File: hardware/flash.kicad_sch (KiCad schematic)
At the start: 2 parts, among them U1 ECP5U_12_CABGA256, U11 W25Q128JVS

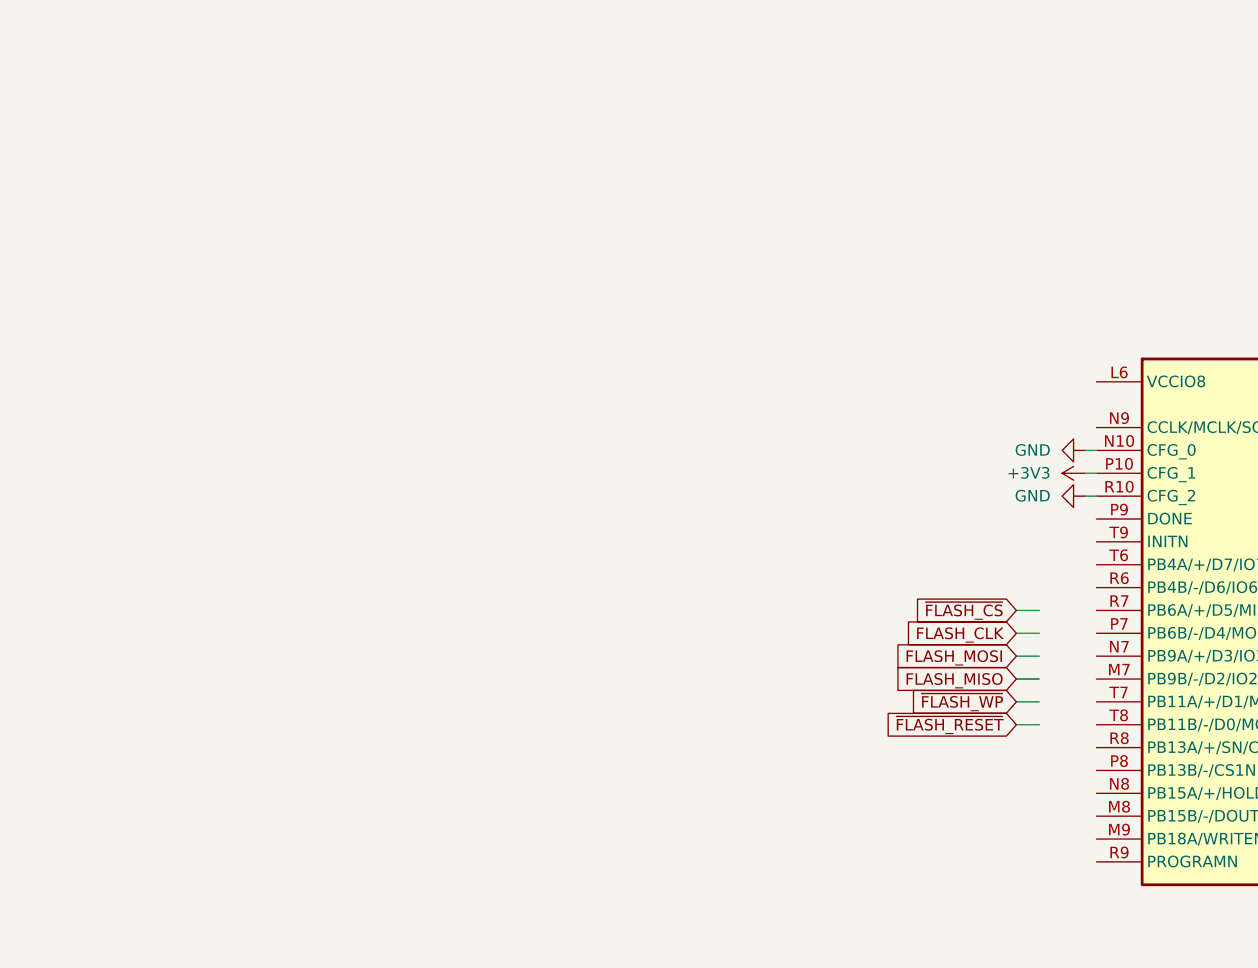
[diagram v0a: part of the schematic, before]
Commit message: Routed most of sdram
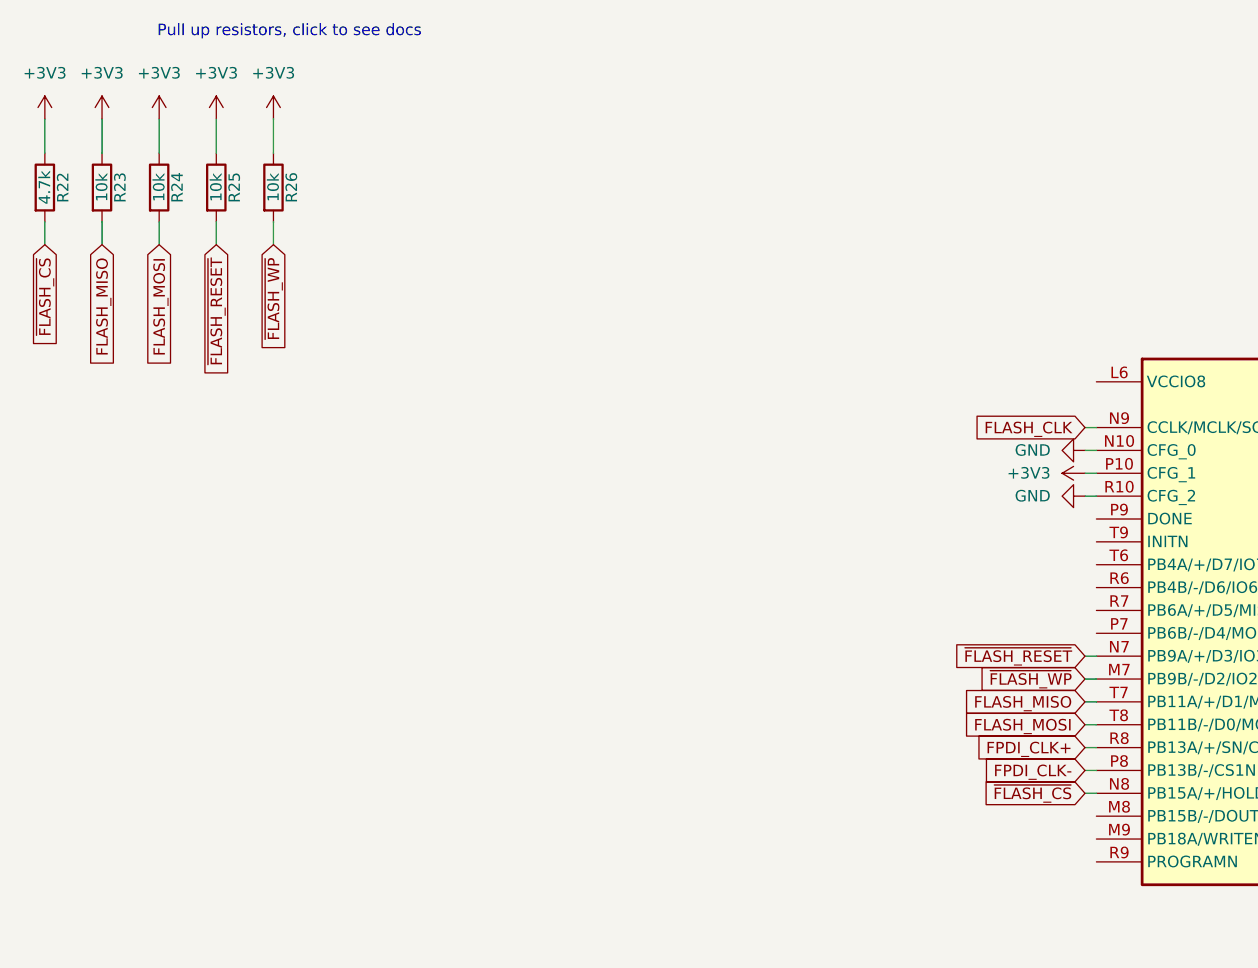
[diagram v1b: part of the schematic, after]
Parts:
- added R22: 4.7k, Resistor_SMD:R_0402_1005Metric, symbol Device:R
- added R23, R24, R25, R26: 10k, Resistor_SMD:R_0402_1005Metric, symbol Device:R
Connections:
- net +3V3: now also R22.1, R23.1, R24.1, R25.1, R26.1
- net FLASH_CLK: now also U1.N9 (CCLK/MCLK/SCK)
- net FLASH_MISO: now also U1.T7 (PB11A/+/D1/MISO/IO1), R23.2
- net FLASH_MOSI: now also U1.T8 (PB11B/-/D0/MOSI/IO0), R24.2
- net ~{FLASH_CS}: now also U1.N8 (PB15A/+/HOLDN/DI/BUSY/CSSPIN/CEN), R22.2
- net ~{FLASH_RESET}: now also U1.N7 (PB9A/+/D3/IO3), R25.2
- net ~{FLASH_WP}: now also U1.M7 (PB9B/-/D2/IO2), R26.2
- net FPDI_CLK-: now reaches U1.P8 (PB13B/-/CS1N)
- net FPDI_CLK+: now reaches U1.R8 (PB13A/+/SN/CSN)
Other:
- note added: "Pull up resistors, click to see docs"

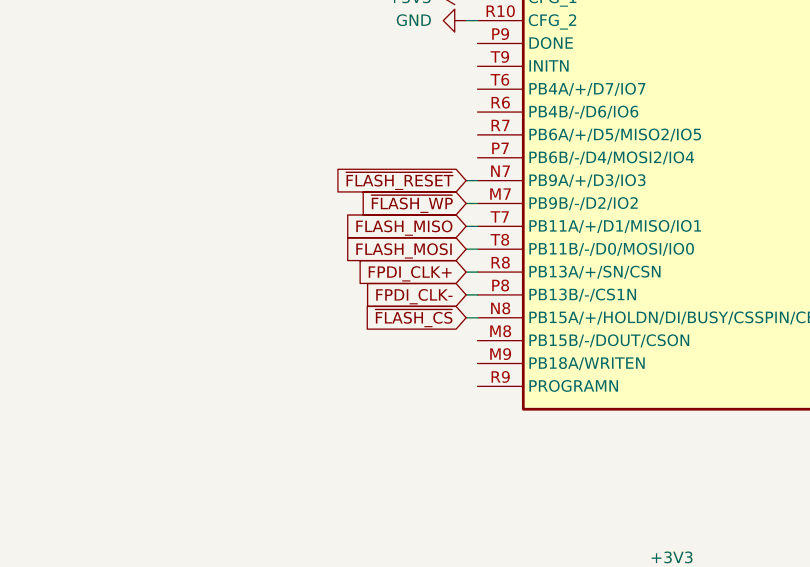
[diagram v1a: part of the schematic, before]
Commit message: Routed power
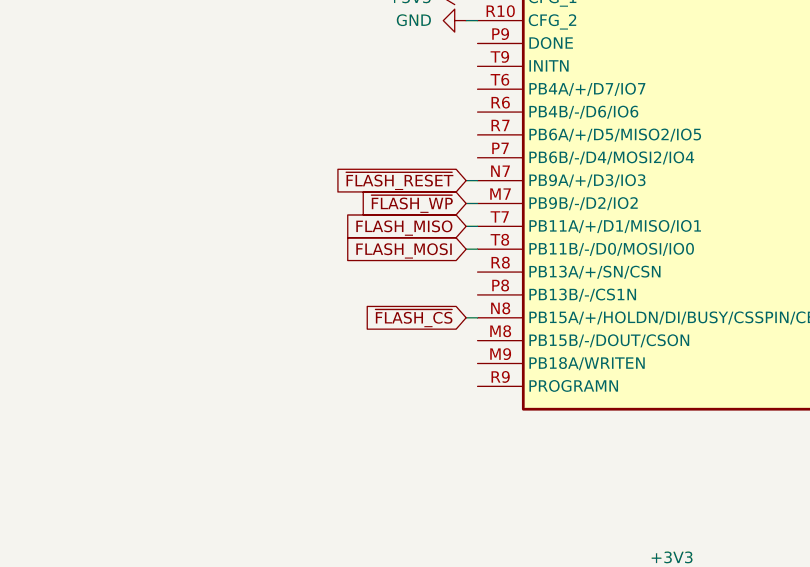
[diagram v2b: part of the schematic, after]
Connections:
- net FPDI_CLK+: no longer names the net of U1.R8 (PB13A/+/SN/CSN)
- net FPDI_CLK-: no longer names the net of U1.P8 (PB13B/-/CS1N)
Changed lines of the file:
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@@
 	(wire
 		(pts
-			(xy 140.97 99.06) (xy 142.24 99.06)
+			(xy 140.97 66.04) (xy 142.24 66.04)
 		)
 		(stroke
@@
 	(wire
 		(pts
-			(xy 140.97 96.52) (xy 142.24 96.52)
+			(xy 151.13 139.7) (xy 153.67 139.7)
 		)
 		(stroke
@@
 	(wire
 		(pts
-			(xy 140.97 66.04) (xy 142.24 66.04)
+			(xy 140.97 63.5) (xy 142.24 63.5)
 		)
 		(stroke
@@
 		)
 	)
-	(wire
-		(pts
-			(xy 151.13 139.7) (xy 153.67 139.7)
-		)
-		(stroke
-			(width 0)
-			(type default)
-		)
-	)
-	(wire
-		(pts
-			(xy 140.97 63.5) (xy 142.24 63.5)
-		)
-		(stroke
-			(width 0)
-			(type default)
-		)
-	)
-	(global_label "FPDI_CLK-"
-		(shape input)
-		(at 140.97 99.06 180)
-		(fields_autoplaced yes)
-		(effects
-			(font
-				(size 1.27 1.27)
-			)
-			(justify right)
-		)
-		(property "Intersheetrefs" "${INTERSHEET_REFS}"
-			(at 127.6433 99.06 0)
-			(effects
-				(font
-					(size 1.27 1.27)
-				)
-				(justify right)
-				(hide yes)
-			)
-		)
-	)
 	(global_label "FLASH_CLK"
 		(shape input)
@@
 			(effects
 				(font
-					(size 1.27 1.27)
-				)
-				(justify right)
-				(hide yes)
-			)
-		)
-	)
-	(global_label "FPDI_CLK+"
-		(shape input)
-		(at 140.97 96.52 180)
-		(fields_autoplaced yes)
-		(effects
-			(font
-				(size 1.27 1.27)
-			)
-			(justify right)
-		)
-		(property "Intersheetrefs" "${INTERSHEET_REFS}"
-			(at 127.6433 96.52 0)
-			(effects
-				(font

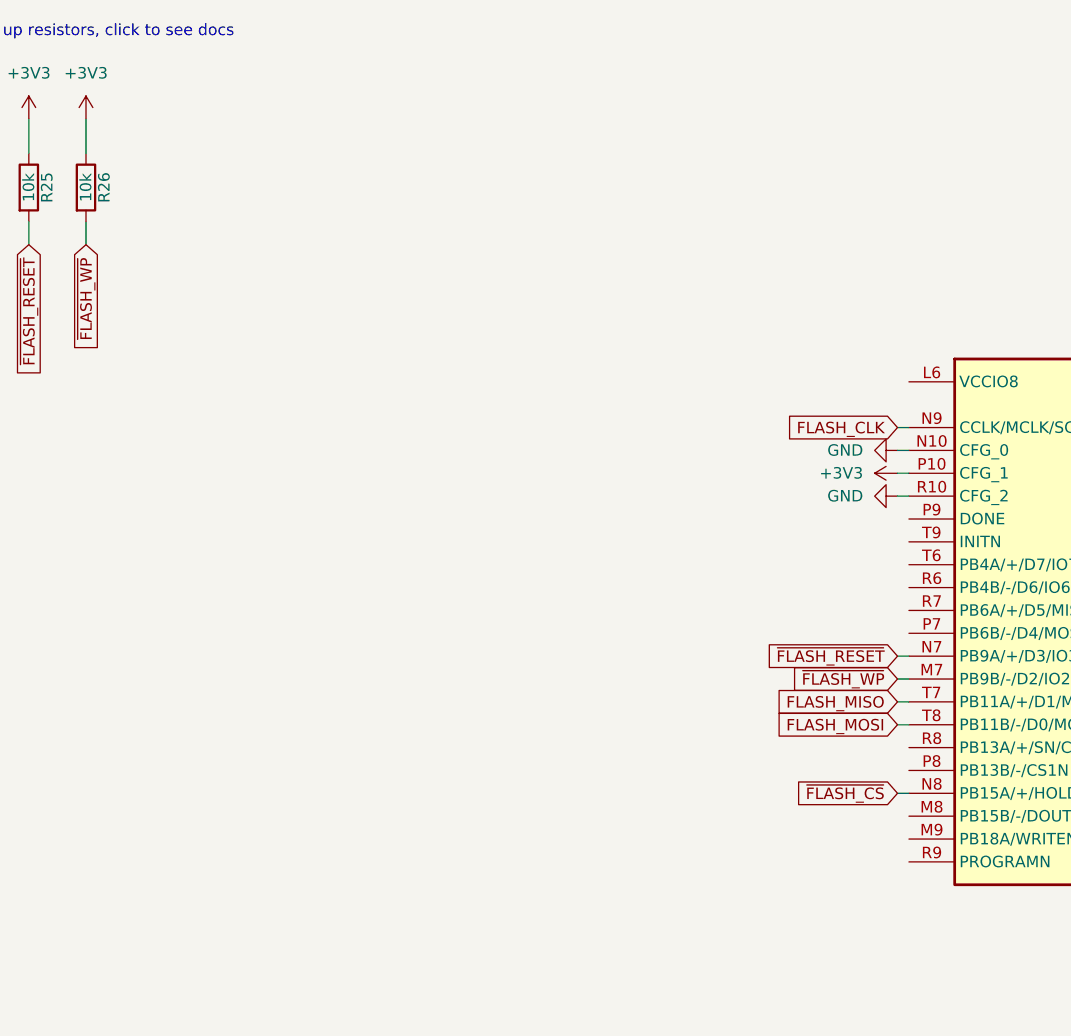
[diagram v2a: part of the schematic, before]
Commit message: Added the decoupling capacitors
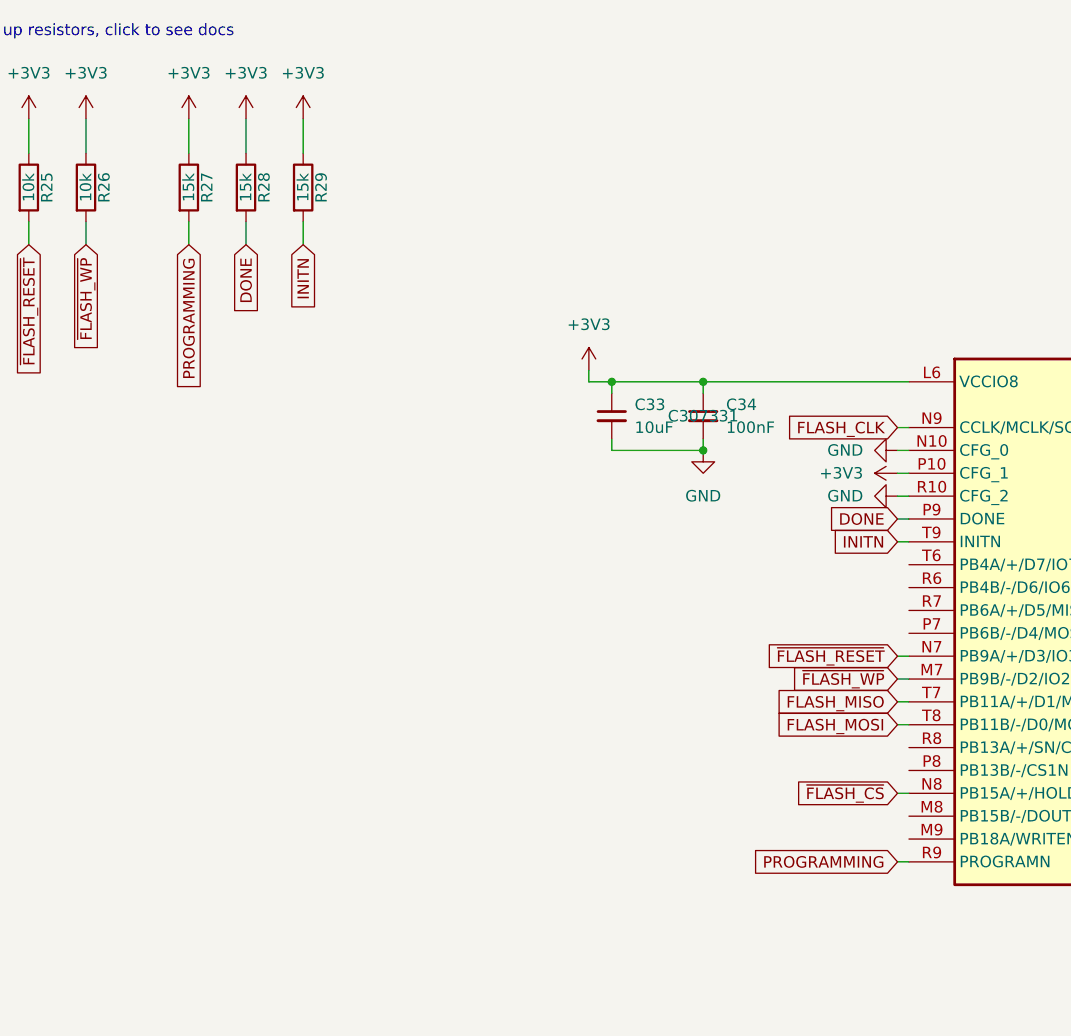
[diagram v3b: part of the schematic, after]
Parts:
- added C33: 10uF, Capacitor_SMD:C_0603_1608Metric, symbol Device:C_Small
- added C34: 100nF, Capacitor_SMD:C_0402_1005Metric, symbol Device:C_Small
- added R27, R28, R29: 15k, Resistor_SMD:R_0402_1005Metric, symbol Device:R
- R22: JLCPCB Part # (none) -> C25900
- R23, R24, R25, R26: JLCPCB Part # (none) -> C25744
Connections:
- net +3V3: now also U1.L6 (VCCIO8), C33.1, C34.1, R27.1, R28.1, R29.1
- net GND: now also C33.2, C34.2
- net DONE: now reaches U1.P9 (DONE)
- net DONE: now also R28.2
- net PROGRAMMING: now reaches U1.R9 (PROGRAMN)
- net PROGRAMMING: now also R27.2
- net INITN: now reaches U1.T9 (INITN)
- net INITN: now also R29.2

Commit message: V1.0 Final Revision and Readme documentation
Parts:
- added C38: 10uF, Capacitor_SMD:C_0603_1608Metric, symbol Device:C_Small
- added J6: Micro_SD_Card_Det2, icepi-lib:microSD_HC_SOFNG_TF-008, symbol Connector:Micro_SD_Card_Det2
- renumbered C33 to C36, C34 to C37, R22 to R26, R23 to R27, R24 to R28, R25 to R29, R26 to R30, R27 to R31, R28 to R32, R29 to R33, U1 to U3
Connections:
- net +3V3: now also C38.1, J6.4 (VDD)
- net GND: now also C38.2, J6.11 (SHIELD), J6.6 (VSS), J6.9 (DET_B)
- new net SD_CLK: J6.5 (CLK)
- new net SD_CMD: J6.3 (CMD)
- new net SD_DAT0: J6.7 (DAT0)
- new net SD_DAT1: J6.8 (DAT1)
- new net SD_DAT2: J6.1 (DAT2)
- new net SD_DAT3: J6.2 (DAT3/CD)
- new net SD_DET: J6.10 (DET_A)
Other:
- moved on the sheet: C36, C37, R26, R27, R28, R29, R30, R31, R32, R33, U11, U3H

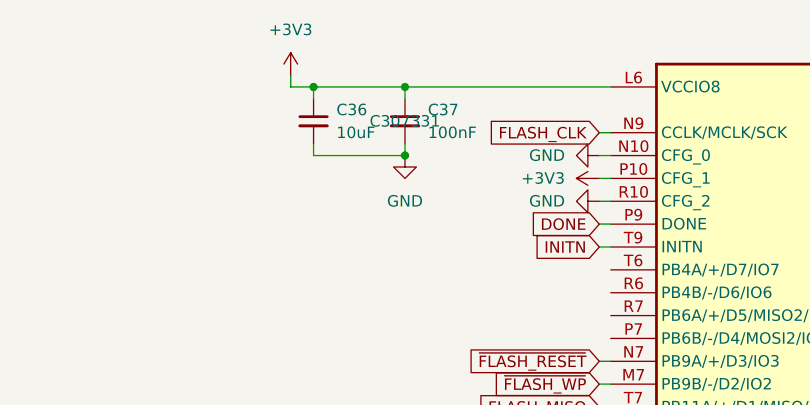
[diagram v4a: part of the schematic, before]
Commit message: Fix level shifter EN voltage error
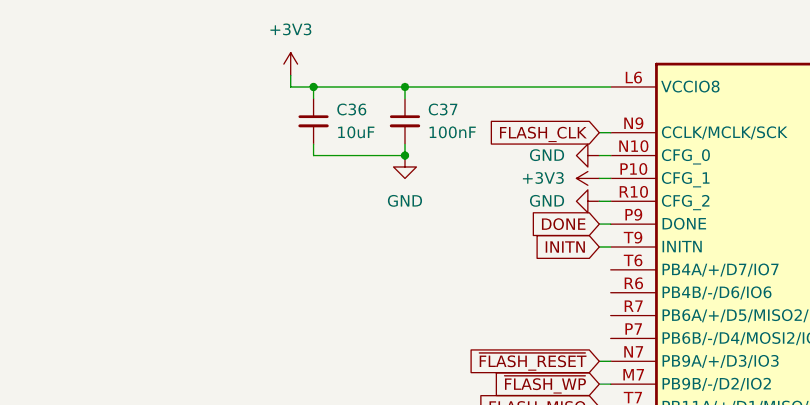
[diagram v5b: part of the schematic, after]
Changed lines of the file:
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@@
 					(size 1.27 1.27)
 				)
+				(hide yes)
 			)
 		)

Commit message: Final revision
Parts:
- C37: JLCPCB Part # C307331 -> (none); LCSC Part # (none) -> C307331
- J6: JLCPCB Part # C428465 -> (none); LCSC Part # (none) -> C428465
- R26: JLCPCB Part # C25900 -> (none); LCSC Part # (none) -> C25900
- R27, R28, R29, R30: JLCPCB Part # C25744 -> (none); LCSC Part # (none) -> C25744
- R31, R32, R33: JLCPCB Part # C25756 -> (none); LCSC Part # (none) -> C25756
- U11: JLCPCB Part # C97521 -> (none); LCSC Part # (none) -> C97521
- U3: JLCPCB Part # C1521614 -> (none); LCSC Part # (none) -> C1521614
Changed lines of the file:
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@@
 			)
 		)
-		(property "JLCPCB Part #" "C307331 "
+		(property "LCSC Part #" "C307331 "
 			(at 165.1 52.07 0)
 			(effects
@@
 					(size 1.27 1.27)
 				)
-				(hide yes)
 			)
 		)
@@
 			)
 		)
-		(property "JLCPCB Part #" "C97521"
+		(property "LCSC Part #" "C97521"
 			(at 209.55 139.7 0)
 			(effects
@@
 					(size 1.27 1.27)
 				)
-				(hide yes)
 			)
 		)
@@
 			)
 		)
-		(property "JLCPCB Part #" "C25756 "
+		(property "LCSC Part #" "C25756 "
 			(at 101.6 64.77 0)
 			(effects
@@
 					(size 1.27 1.27)
 				)
-				(hide yes)
 			)
 		)
@@
 			)
 		)
-		(property "JLCPCB Part #" "C25756 "
+		(property "LCSC Part #" "C25756 "
 			(at 107.95 64.77 0)
 			(effects
@@
 					(size 1.27 1.27)
 				)
-				(hide yes)
 			)
 		)
@@
 			)
 		)
-		(property "JLCPCB Part #" "C1521614"
+		(property "LCSC Part #" "C1521614"
 			(at 209.55 86.36 0)
 			(effects
@@
 					(size 1.27 1.27)
 				)
-				(hide yes)
 			)
 		)
@@
 			)
 		)
-		(property "JLCPCB Part #" "C25744"
+		(property "LCSC Part #" "C25744"
 			(at 83.82 64.77 0)
 			(effects
@@
 					(size 1.27 1.27)
 				)
-				(hide yes)
 			)
 		)
@@
 			)
 		)
-		(property "JLCPCB Part #" "C25756 "
+		(property "LCSC Part #" "C25756 "
 			(at 114.3 64.77 0)
 			(effects
@@
 					(size 1.27 1.27)
 				)
-				(hide yes)
 			)
 		)
@@
 			)
 		)
-		(property "JLCPCB Part #" "C25900 "
+		(property "LCSC Part #" "C25900 "
 			(at 64.77 64.77 0)
 			(effects
@@
 					(size 1.27 1.27)
 				)
-				(hide yes)
 			)
 		)
@@
 			)
 		)
-		(property "JLCPCB Part #" "C25744"
+		(property "LCSC Part #" "C25744"
 			(at 71.12 64.77 0)
 			(effects
@@
 					(size 1.27 1.27)
 				)
-				(hide yes)
 			)
 		)
@@
 			)
 		)
-		(property "JLCPCB Part #" "C25744"
+		(property "LCSC Part #" "C25744"
 			(at 90.17 64.77 0)
 			(effects
@@
 					(size 1.27 1.27)
 				)
-				(hide yes)
 			)
 		)
@@
 			)
 		)
-		(property "JLCPCB Part #" "C428465"
+		(property "LCSC Part #" "C428465"
 			(at 99.06 129.54 0)
 			(effects
@@
 					(size 1.27 1.27)
 				)
-				(hide yes)
 			)
 		)
@@
 			)
 		)
-		(property "JLCPCB Part #" "C25744"
+		(property "LCSC Part #" "C25744"
 			(at 77.47 64.77 0)
 			(effects
@@
 					(size 1.27 1.27)
 				)
-				(hide yes)
-			)
-		)
+			)
+		)

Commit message: Last checks
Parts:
- C45: renamed from C36; LCSC Part # (none) -> C19702
- C47: renamed from C38; LCSC Part # (none) -> C19702
- renumbered C37 to C46, R26 to R31, R27 to R32, R28 to R33, R29 to R34, R30 to R35, R31 to R36, R32 to R37, R33 to R38, U3 to U1
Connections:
- no-connect marks 0 -> 8
